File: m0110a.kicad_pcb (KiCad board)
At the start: 2 copper layers, 177 parts, among them SW1 SW_Push, U1 ATmega32U4-AU, Y1 16MHz

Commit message: fix foot print associations. place switch foot prints and some diodes
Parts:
- removed C1, C2: 22pF, Capacitor_SMD:C_0805_2012Metric
- removed C3: 1uF, Capacitor_SMD:C_0805_2012Metric
- removed C4, C5, C6: 0.1uF, Capacitor_SMD:C_0805_2012Metric
- removed C7: 10uF, Capacitor_SMD:C_0805_2012Metric
- removed D80: D_Small, Diode_SMD:D_SOD-123
- removed F1: 500mA, Fuse:Fuse_1206_3216Metric
- removed MX_1, MX_2, MX_3, MX_4, MX_5, MX_6, MX_7, MX_8, MX_9, MX_A1, MX_B1, MX_BSLSH1, MX_C1, MX_COMMA1, MX_D1, MX_DOT1, MX_DWN1, MX_E1, MX_EQL1, MX_ESC1, MX_F1, MX_FN1, MX_G1, MX_H1, MX_I1, MX_J1, MX_K1, MX_L1, MX_LBRC1, MX_LEFT1, MX_M1, MX_MINS1, MX_N1, MX_NUM1, MX_NUM_0, MX_NUM_1, MX_NUM_2, MX_NUM_3, MX_NUM_4, MX_NUM_5, MX_NUM_6, MX_NUM_7, MX_NUM_8, MX_NUM_9, MX_NUM_ADD1, MX_NUM_DBL_0, MX_NUM_DOT1, MX_NUM_EQL1, MX_NUM_MINS1, MX_NUM_MUL1, MX_NUM_SLSH1, MX_O1, MX_P1, MX_Q1, MX_QUOT1, MX_R1, MX_RBRC1, MX_RIGHT1, MX_S1, MX_SEMI1, MX_SLSH1, MX_T1, MX_U1, MX_UP1, MX_V1, MX_W1, MX_X1, MX_Y1, MX_Z1, MX_ZERO1: MX-LED, MX_Alps_Hybrid:MX-1U
- removed MX_7U_SPC1: MX-LED, MX_Alps_Hybrid:MX-7U
- removed MX_BSPC1, MX_LALT1, MX_TAB1: MX-LED, MX_Alps_Hybrid:MX-1.5U
- removed MX_CAP1, MX_ENTER1: MX-LED, MX_Alps_Hybrid:MX-1.75U
- removed MX_LGUI1, MX_NUM_BIG_0, MX_NUM_ENT1: MX-LED, MX_Alps_Hybrid:MX-2U
- removed MX_LSFT1: MX-LED, MX_Alps_Hybrid:MX-2.25U
- removed MX_RSFT1: MX-LED, MX_Alps_Hybrid:MX-1.25U
- removed R1, R4: 10k, Resistor_SMD:R_0805_2012Metric
- removed R2, R3: 22, Resistor_SMD:R_0805_2012Metric
- removed SW1: SW_Push, random-keyboard-parts:SKQG-1155865
- removed USB1: Molex-0548190589, random-keyboard-parts:Molex-0548190589
- removed Y1: 16MHz, Crystal:Crystal_SMD_3225-4Pin_3.2x2.5mm
- added MX1: CherryMX_LTST-A683CEGBW, CherryMX_PCB_KailhSocket_LTST-A683CEGBW:CherryMX_1.00u_PCB_KailhSocket_LTST-A683CEGBW, F.Cu at (95.2, 0.00)
- added MX10: CherryMX_LTST-A683CEGBW, CherryMX_PCB_KailhSocket_LTST-A683CEGBW:CherryMX_1.00u_PCB_KailhSocket_LTST-A683CEGBW, F.Cu at (57.1, 0.00)
- added MX11: CherryMX_LTST-A683CEGBW, CherryMX_PCB_KailhSocket_LTST-A683CEGBW:CherryMX_1.00u_PCB_KailhSocket_LTST-A683CEGBW, F.Cu at (209.6, 0.00)
- added MX12: CherryMX_LTST-A683CEGBW, CherryMX_PCB_KailhSocket_LTST-A683CEGBW:CherryMX_1.50u_PCB_KailhSocket_LTST-A683CEGBW, F.Cu at (252.4, 0.00)
- added MX13: CherryMX_LTST-A683CEGBW, CherryMX_PCB_KailhSocket_LTST-A683CEGBW:CherryMX_1.00u_PCB_KailhSocket_LTST-A683CEGBW, F.Cu at (301.6, 0.00)
- added MX14: CherryMX_LTST-A683CEGBW, CherryMX_PCB_KailhSocket_LTST-A683CEGBW:CherryMX_1.00u_PCB_KailhSocket_LTST-A683CEGBW, F.Cu at (339.7, 0.00)
- added MX15: CherryMX_LTST-A683CEGBW, CherryMX_PCB_KailhSocket_LTST-A683CEGBW:CherryMX_1.00u_PCB_KailhSocket_LTST-A683CEGBW, F.Cu at (19.1, 0.00)
- added MX16: CherryMX_LTST-A683CEGBW, CherryMX_PCB_KailhSocket_LTST-A683CEGBW:CherryMX_1.00u_PCB_KailhSocket_LTST-A683CEGBW, F.Cu at (38.1, 0.00)
- added MX17: CherryMX_LTST-A683CEGBW, CherryMX_PCB_KailhSocket_LTST-A683CEGBW:CherryMX_1.00u_PCB_KailhSocket_LTST-A683CEGBW, F.Cu at (228.6, 0.00)
- added MX18: CherryMX_LTST-A683CEGBW, CherryMX_PCB_KailhSocket_LTST-A683CEGBW:CherryMX_1.00u_PCB_KailhSocket_LTST-A683CEGBW, F.Cu at (0.00, 0.00)
- added MX19: CherryMX_LTST-A683CEGBW, CherryMX_PCB_KailhSocket_LTST-A683CEGBW:CherryMX_1.00u_PCB_KailhSocket_LTST-A683CEGBW, F.Cu at (104.8, 19.1)
- added MX2: CherryMX_LTST-A683CEGBW, CherryMX_PCB_KailhSocket_LTST-A683CEGBW:CherryMX_1.00u_PCB_KailhSocket_LTST-A683CEGBW, F.Cu at (114.3, 0.00)
- added MX20: CherryMX_LTST-A683CEGBW, CherryMX_PCB_KailhSocket_LTST-A683CEGBW:CherryMX_1.00u_PCB_KailhSocket_LTST-A683CEGBW, F.Cu at (123.8, 19.1)
- added MX21: CherryMX_LTST-A683CEGBW, CherryMX_PCB_KailhSocket_LTST-A683CEGBW:CherryMX_1.00u_PCB_KailhSocket_LTST-A683CEGBW, F.Cu at (142.9, 19.1)
- added MX22: CherryMX_LTST-A683CEGBW, CherryMX_PCB_KailhSocket_LTST-A683CEGBW:CherryMX_1.00u_PCB_KailhSocket_LTST-A683CEGBW, F.Cu at (161.9, 19.1)
- added MX23: CherryMX_LTST-A683CEGBW, CherryMX_PCB_KailhSocket_LTST-A683CEGBW:CherryMX_1.00u_PCB_KailhSocket_LTST-A683CEGBW, F.Cu at (181.0, 19.1)
- added MX24: CherryMX_LTST-A683CEGBW, CherryMX_PCB_KailhSocket_LTST-A683CEGBW:CherryMX_1.00u_PCB_KailhSocket_LTST-A683CEGBW, F.Cu at (200.0, 19.1)
- added MX25: CherryMX_LTST-A683CEGBW, CherryMX_PCB_KailhSocket_LTST-A683CEGBW:CherryMX_1.00u_PCB_KailhSocket_LTST-A683CEGBW, F.Cu at (85.7, 19.1)
- added MX26: CherryMX_LTST-A683CEGBW, CherryMX_PCB_KailhSocket_LTST-A683CEGBW:CherryMX_1.00u_PCB_KailhSocket_LTST-A683CEGBW, F.Cu at (282.6, 19.1)
- added MX27: CherryMX_LTST-A683CEGBW, CherryMX_PCB_KailhSocket_LTST-A683CEGBW:CherryMX_1.00u_PCB_KailhSocket_LTST-A683CEGBW, F.Cu at (320.7, 19.1)
- added MX28: CherryMX_LTST-A683CEGBW, CherryMX_PCB_KailhSocket_LTST-A683CEGBW:CherryMX_1.00u_PCB_KailhSocket_LTST-A683CEGBW, F.Cu at (66.7, 19.1)
- added MX29: CherryMX_LTST-A683CEGBW, CherryMX_PCB_KailhSocket_LTST-A683CEGBW:CherryMX_1.00u_PCB_KailhSocket_LTST-A683CEGBW, F.Cu at (219.1, 19.1)
- added MX3: CherryMX_LTST-A683CEGBW, CherryMX_PCB_KailhSocket_LTST-A683CEGBW:CherryMX_1.00u_PCB_KailhSocket_LTST-A683CEGBW, F.Cu at (133.3, 0.00)
- added MX30: CherryMX_LTST-A683CEGBW, CherryMX_PCB_KailhSocket_LTST-A683CEGBW:CherryMX_1.00u_PCB_KailhSocket_LTST-A683CEGBW, F.Cu at (257.2, 19.1)
- added MX31: CherryMX_LTST-A683CEGBW, CherryMX_PCB_KailhSocket_LTST-A683CEGBW:CherryMX_1.00u_PCB_KailhSocket_LTST-A683CEGBW, F.Cu at (301.6, 19.1)
- added MX32: CherryMX_LTST-A683CEGBW, CherryMX_PCB_KailhSocket_LTST-A683CEGBW:CherryMX_1.00u_PCB_KailhSocket_LTST-A683CEGBW, F.Cu at (339.7, 19.1)
- added MX33: CherryMX_LTST-A683CEGBW, CherryMX_PCB_KailhSocket_LTST-A683CEGBW:CherryMX_1.00u_PCB_KailhSocket_LTST-A683CEGBW, F.Cu at (28.6, 19.1)
- added MX34: CherryMX_LTST-A683CEGBW, CherryMX_PCB_KailhSocket_LTST-A683CEGBW:CherryMX_1.00u_PCB_KailhSocket_LTST-A683CEGBW, F.Cu at (47.6, 19.1)
- added MX35: CherryMX_LTST-A683CEGBW, CherryMX_PCB_KailhSocket_LTST-A683CEGBW:CherryMX_1.00u_PCB_KailhSocket_LTST-A683CEGBW, F.Cu at (238.1, 19.1)
- added MX36: CherryMX_LTST-A683CEGBW, CherryMX_PCB_KailhSocket_LTST-A683CEGBW:CherryMX_1.50u_PCB_KailhSocket_LTST-A683CEGBW, F.Cu at (4.76, 19.1)
- added MX37: CherryMX_LTST-A683CEGBW, CherryMX_PCB_KailhSocket_LTST-A683CEGBW:CherryMX_1.00u_PCB_KailhSocket_LTST-A683CEGBW, F.Cu at (147.6, 38.1)
- added MX38: CherryMX_LTST-A683CEGBW, CherryMX_PCB_KailhSocket_LTST-A683CEGBW:CherryMX_1.00u_PCB_KailhSocket_LTST-A683CEGBW, F.Cu at (109.5, 38.1)
- added MX39: CherryMX_LTST-A683CEGBW, CherryMX_PCB_KailhSocket_LTST-A683CEGBW:CherryMX_1.00u_PCB_KailhSocket_LTST-A683CEGBW, F.Cu at (128.6, 38.1)
- added MX4: CherryMX_LTST-A683CEGBW, CherryMX_PCB_KailhSocket_LTST-A683CEGBW:CherryMX_1.00u_PCB_KailhSocket_LTST-A683CEGBW, F.Cu at (152.4, 0.00)
- added MX40: CherryMX_LTST-A683CEGBW, CherryMX_PCB_KailhSocket_LTST-A683CEGBW:CherryMX_1.00u_PCB_KailhSocket_LTST-A683CEGBW, F.Cu at (166.7, 38.1)
- added MX41: CherryMX_LTST-A683CEGBW, CherryMX_PCB_KailhSocket_LTST-A683CEGBW:CherryMX_1.00u_PCB_KailhSocket_LTST-A683CEGBW, F.Cu at (185.7, 38.1)
- added MX42: CherryMX_LTST-A683CEGBW, CherryMX_PCB_KailhSocket_LTST-A683CEGBW:CherryMX_1.00u_PCB_KailhSocket_LTST-A683CEGBW, F.Cu at (204.8, 38.1)
- added MX43: CherryMX_LTST-A683CEGBW, CherryMX_PCB_KailhSocket_LTST-A683CEGBW:CherryMX_1.00u_PCB_KailhSocket_LTST-A683CEGBW, F.Cu at (90.5, 38.1)
- added MX44: CherryMX_LTST-A683CEGBW, CherryMX_PCB_KailhSocket_LTST-A683CEGBW:CherryMX_1.00u_PCB_KailhSocket_LTST-A683CEGBW, F.Cu at (282.6, 38.1)
- added MX45: CherryMX_LTST-A683CEGBW, CherryMX_PCB_KailhSocket_LTST-A683CEGBW:CherryMX_1.00u_PCB_KailhSocket_LTST-A683CEGBW, F.Cu at (320.7, 38.1)
- added MX46: CherryMX_LTST-A683CEGBW, CherryMX_PCB_KailhSocket_LTST-A683CEGBW:CherryMX_1.00u_PCB_KailhSocket_LTST-A683CEGBW, F.Cu at (71.4, 38.1)
- added MX47: CherryMX_LTST-A683CEGBW, CherryMX_PCB_KailhSocket_LTST-A683CEGBW:CherryMX_1.00u_PCB_KailhSocket_LTST-A683CEGBW, F.Cu at (223.8, 38.1)
- added MX48: CherryMX_LTST-A683CEGBW, CherryMX_PCB_KailhSocket_LTST-A683CEGBW:CherryMX_1.75u_PCB_KailhSocket_LTST-A683CEGBW, F.Cu at (250.0, 38.1)
- added MX49: CherryMX_LTST-A683CEGBW, CherryMX_PCB_KailhSocket_LTST-A683CEGBW:CherryMX_1.00u_PCB_KailhSocket_LTST-A683CEGBW, F.Cu at (301.6, 38.1)
- added MX5: CherryMX_LTST-A683CEGBW, CherryMX_PCB_KailhSocket_LTST-A683CEGBW:CherryMX_1.00u_PCB_KailhSocket_LTST-A683CEGBW, F.Cu at (171.4, 0.00)
- added MX50: CherryMX_LTST-A683CEGBW, CherryMX_PCB_KailhSocket_LTST-A683CEGBW:CherryMX_1.00u_PCB_KailhSocket_LTST-A683CEGBW, F.Cu at (339.7, 38.1)
- added MX51: CherryMX_LTST-A683CEGBW, CherryMX_PCB_KailhSocket_LTST-A683CEGBW:CherryMX_1.00u_PCB_KailhSocket_LTST-A683CEGBW, F.Cu at (33.3, 38.1)
- added MX52: CherryMX_LTST-A683CEGBW, CherryMX_PCB_KailhSocket_LTST-A683CEGBW:CherryMX_1.00u_PCB_KailhSocket_LTST-A683CEGBW, F.Cu at (52.4, 38.1)
- added MX53: CherryMX_LTST-A683CEGBW, CherryMX_PCB_KailhSocket_LTST-A683CEGBW:CherryMX_1.75u_PCB_KailhSocket_LTST-A683CEGBW, F.Cu at (7.14, 38.1)
- added MX54: CherryMX_LTST-A683CEGBW, CherryMX_PCB_KailhSocket_LTST-A683CEGBW:CherryMX_1.00u_PCB_KailhSocket_LTST-A683CEGBW, F.Cu at (157.2, 57.1)
- added MX55: CherryMX_LTST-A683CEGBW, CherryMX_PCB_KailhSocket_LTST-A683CEGBW:CherryMX_1.00u_PCB_KailhSocket_LTST-A683CEGBW, F.Cu at (119.1, 57.1)
- added MX56: CherryMX_LTST-A683CEGBW, CherryMX_PCB_KailhSocket_LTST-A683CEGBW:CherryMX_1.00u_PCB_KailhSocket_LTST-A683CEGBW, F.Cu at (138.1, 57.1)
- added MX57: CherryMX_LTST-A683CEGBW, CherryMX_PCB_KailhSocket_LTST-A683CEGBW:CherryMX_1.00u_PCB_KailhSocket_LTST-A683CEGBW, F.Cu at (176.2, 57.1)
- added MX58: CherryMX_LTST-A683CEGBW, CherryMX_PCB_KailhSocket_LTST-A683CEGBW:CherryMX_1.00u_PCB_KailhSocket_LTST-A683CEGBW, F.Cu at (195.3, 57.1)
- added MX59: CherryMX_LTST-A683CEGBW, CherryMX_PCB_KailhSocket_LTST-A683CEGBW:CherryMX_1.00u_PCB_KailhSocket_LTST-A683CEGBW, F.Cu at (214.3, 57.1)
- added MX6: CherryMX_LTST-A683CEGBW, CherryMX_PCB_KailhSocket_LTST-A683CEGBW:CherryMX_1.00u_PCB_KailhSocket_LTST-A683CEGBW, F.Cu at (190.5, 0.00)
- added MX60: CherryMX_LTST-A683CEGBW, CherryMX_PCB_KailhSocket_LTST-A683CEGBW:CherryMX_1.00u_PCB_KailhSocket_LTST-A683CEGBW, F.Cu at (100.0, 57.1)
- added MX61: CherryMX_LTST-A683CEGBW, CherryMX_PCB_KailhSocket_LTST-A683CEGBW:CherryMX_1.00u_PCB_KailhSocket_LTST-A683CEGBW, F.Cu at (257.2, 57.1)
- added MX62: CherryMX_LTST-A683CEGBW, CherryMX_PCB_KailhSocket_LTST-A683CEGBW:CherryMX_1.00u_PCB_KailhSocket_LTST-A683CEGBW, F.Cu at (282.6, 57.1)
- added MX63: CherryMX_LTST-A683CEGBW, CherryMX_PCB_KailhSocket_LTST-A683CEGBW:CherryMX_1.00u_PCB_KailhSocket_LTST-A683CEGBW, F.Cu at (320.7, 57.1)
- added MX64: CherryMX_LTST-A683CEGBW, CherryMX_PCB_KailhSocket_LTST-A683CEGBW:CherryMX_1.00u_PCB_KailhSocket_LTST-A683CEGBW, F.Cu at (81.0, 57.1)
- added MX65: CherryMX_LTST-A683CEGBW, CherryMX_PCB_KailhSocket_LTST-A683CEGBW:CherryMX_1.00u_PCB_KailhSocket_LTST-A683CEGBW, F.Cu at (301.6, 57.1)
- added MX66: CherryMX_LTST-A683CEGBW, CherryMX_PCB_KailhSocket_LTST-A683CEGBW:CherryMX_1.00u_PCB_KailhSocket_LTST-A683CEGBW, F.Cu at (42.9, 57.1)
- added MX67: CherryMX_LTST-A683CEGBW, CherryMX_PCB_KailhSocket_LTST-A683CEGBW:CherryMX_1.00u_PCB_KailhSocket_LTST-A683CEGBW, F.Cu at (61.9, 57.1)
- added MX68: CherryMX_LTST-A683CEGBW, CherryMX_PCB_KailhSocket_LTST-A683CEGBW:CherryMX_1.25u_PCB_KailhSocket_LTST-A683CEGBW, F.Cu at (235.7, 57.1)
- added MX69: CherryMX_LTST-A683CEGBW, CherryMX_PCB_KailhSocket_StabWireBottom_LTST-A683CEGBW:CherryMX_2.25u_PCB_KailhSocket_StabWireBottom_LTST-A683CEGBW, F.Cu at (11.9, 57.1)
- added MX7: CherryMX_LTST-A683CEGBW, CherryMX_PCB_KailhSocket_LTST-A683CEGBW:CherryMX_1.00u_PCB_KailhSocket_LTST-A683CEGBW, F.Cu at (76.2, 0.00)
- added MX70: CherryMX_LTST-A683CEGBW, CherryMX_PCB_KailhSocket_StabWireBottom_LTST-A683CEGBW:CherryMX_2.00u_PCB_KailhSocket_StabWireBottom_LTST-A683CEGBW, F.Cu at (339.7, 66.7)
- added MX71: CherryMX_LTST-A683CEGBW, CherryMX_PCB_KailhSocket_StabWireBottom_LTST-A683CEGBW:CherryMX_7.00u_PCB_KailhSocket_StabWireBottom_LTST-A683CEGBW, F.Cu at (123.8, 76.2)
- added MX72: CherryMX_LTST-A683CEGBW, CherryMX_PCB_KailhSocket_LTST-A683CEGBW:CherryMX_1.00u_PCB_KailhSocket_LTST-A683CEGBW, F.Cu at (200.0, 76.2)
- added MX73: CherryMX_LTST-A683CEGBW, CherryMX_PCB_KailhSocket_LTST-A683CEGBW:CherryMX_1.00u_PCB_KailhSocket_LTST-A683CEGBW, F.Cu at (320.7, 76.2)
- added MX74: CherryMX_LTST-A683CEGBW, CherryMX_PCB_KailhSocket_LTST-A683CEGBW:CherryMX_1.00u_PCB_KailhSocket_LTST-A683CEGBW, F.Cu at (219.1, 76.2)
- added MX75: CherryMX_LTST-A683CEGBW, CherryMX_PCB_KailhSocket_LTST-A683CEGBW:CherryMX_1.00u_PCB_KailhSocket_LTST-A683CEGBW, F.Cu at (257.2, 76.2)
- added MX76: CherryMX_LTST-A683CEGBW, CherryMX_PCB_KailhSocket_StabWireBottom_LTST-A683CEGBW:CherryMX_2.00u_PCB_KailhSocket_StabWireBottom_LTST-A683CEGBW, F.Cu at (292.1, 76.2)
- added MX77: CherryMX_LTST-A683CEGBW, CherryMX_PCB_KailhSocket_StabWireBottom_LTST-A683CEGBW:CherryMX_2.00u_PCB_KailhSocket_StabWireBottom_LTST-A683CEGBW, F.Cu at (38.1, 76.2)
- added MX78: CherryMX_LTST-A683CEGBW, CherryMX_PCB_KailhSocket_LTST-A683CEGBW:CherryMX_1.00u_PCB_KailhSocket_LTST-A683CEGBW, F.Cu at (238.1, 76.2)
- added MX79: CherryMX_LTST-A683CEGBW, CherryMX_PCB_KailhSocket_LTST-A683CEGBW:CherryMX_1.50u_PCB_KailhSocket_LTST-A683CEGBW, F.Cu at (4.76, 76.2)
- added MX8: CherryMX_LTST-A683CEGBW, CherryMX_PCB_KailhSocket_LTST-A683CEGBW:CherryMX_1.00u_PCB_KailhSocket_LTST-A683CEGBW, F.Cu at (282.6, 0.00)
- added MX9: CherryMX_LTST-A683CEGBW, CherryMX_PCB_KailhSocket_LTST-A683CEGBW:CherryMX_1.00u_PCB_KailhSocket_LTST-A683CEGBW, F.Cu at (320.7, 0.00)
- U1: value ATmega32U4-AU -> Teensy++2.0_(C); footprint Package_QFP:TQFP-44_10x10mm_P0.8mm -> teensy:Teensy2.0++; moved to F.Cu
- moved D18 344.5 mm to (7.94, 0.79)
- moved D17 306.4 mm to (27.0, 0.79)
- moved D19 276.1 mm to (272.1, 114.4), turned to 0 degrees
- moved D20 255.1 mm to (272.1, 117.8), turned to 0 degrees
- moved D37 246.8 mm to (249.0, 117.7), turned to 0 degrees
- moved D21 246.3 mm to (278.5, 124.5), turned to 0 degrees
- moved D15 230.2 mm to (65.1, 0.79)
- moved D22 224.1 mm to (272.8, 124.5), turned to 0 degrees
- moved D38 216.8 mm to (243.2, 117.7), turned to 0 degrees
- moved D69 214.9 mm to (123.2, 102.6), turned to 0 degrees
- moved D14 214.3 mm to (46.0, 0.79)
- moved D23 214.1 mm to (278.5, 127.9), turned to 0 degrees
- moved D73 205.5 mm to (128.9, 107.2), turned to 0 degrees
- moved D70 204.6 mm to (140.4, 106.0), turned to 0 degrees
- moved D24 199.7 mm to (278.5, 131.2), turned to 0 degrees
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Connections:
- U1 pad 1: Net-(U1-Pad1) -> GND
- U1 pad 14: +5V -> Net-(U1-Pad14)
- U1 pad 15: GND -> Net-(U1-Pad15)
- U1 pad 2: +5V -> Net-(U1-Pad2)
- U1 pad 21: Net-(U1-Pad21) -> VCC
- U1 pad 22: Net-(U1-Pad22) -> GND
- U1 pad 23: GND -> Net-(U1-Pad23)
- U1 pad 24: +5V -> Net-(U1-Pad24)
- U1 pad 33: Net-(R4-Pad2) -> GND
- U1 pad 34: +5V -> Net-(U1-Pad34)
- U1 pad 35: GND -> Net-(U1-Pad35)
- U1 pad 43: GND -> Net-(U1-Pad43)
- U1 pad 44: +5V -> Net-(U1-Pad44)
- U1 pad 5: GND -> Net-(U1-Pad5)
- U1 pad 7: +5V -> Net-(U1-Pad7)
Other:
- board outline added: 3.4 x 3 mm

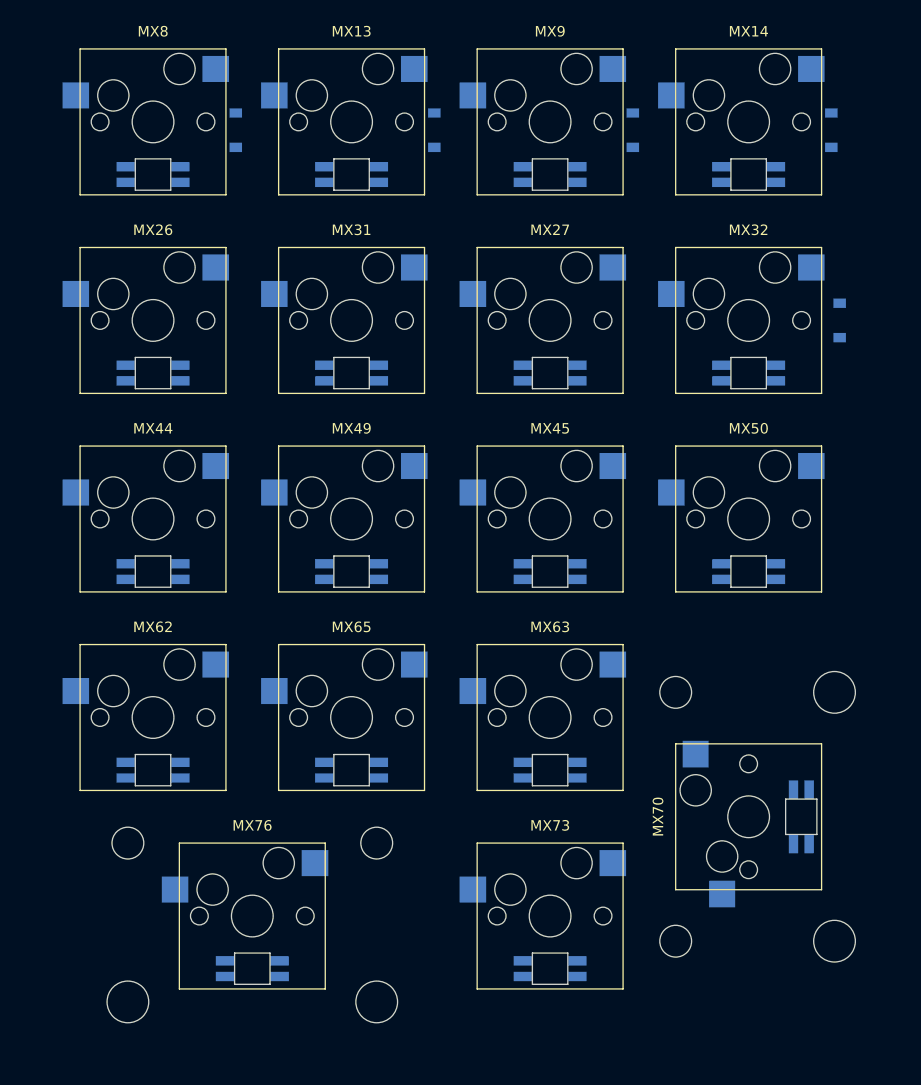
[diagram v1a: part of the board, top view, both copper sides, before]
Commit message: place number pad 34.5mm away from center of back space
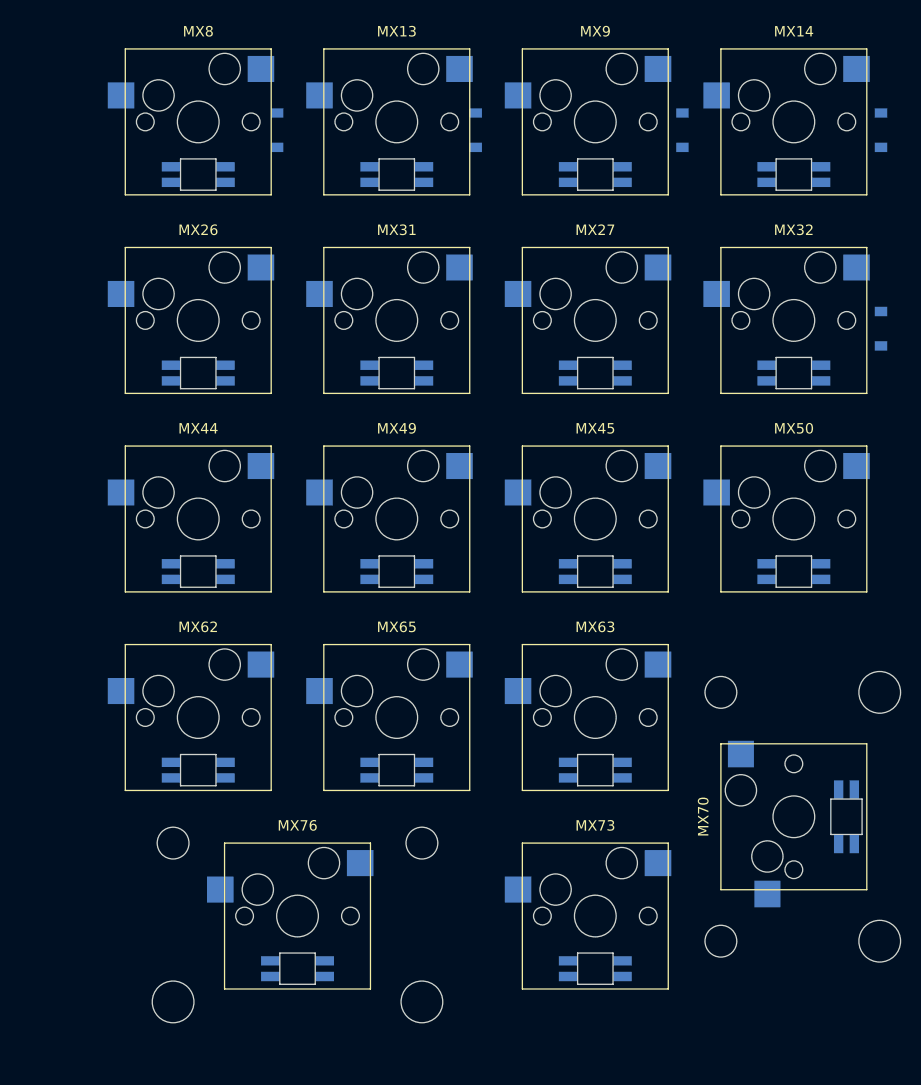
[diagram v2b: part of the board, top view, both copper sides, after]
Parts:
- moved D12 4.76 mm to (352.4, 0.79)
- moved D8 4.76 mm to (333.4, 0.79)
- moved MX26 4.34 mm to (286.9, 19.1)
- moved MX44 4.34 mm to (286.9, 38.1)
- moved MX62 4.34 mm to (286.9, 57.1)
- moved MX8 4.34 mm to (286.9, 0.00)
- moved MX13 4.34 mm to (306.0, 0.00)
- moved MX14 4.34 mm to (344.1, 0.00)
- moved MX27 4.34 mm to (325.0, 19.1)
- moved MX31 4.34 mm to (306.0, 19.1)
- moved MX32 4.34 mm to (344.1, 19.1)
- moved MX45 4.34 mm to (325.0, 38.1)
- moved MX49 4.34 mm to (306.0, 38.1)
- moved MX50 4.34 mm to (344.1, 38.1)
- moved MX63 4.34 mm to (325.0, 57.1)
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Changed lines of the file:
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@@
     (solder_mask_min_width 0.25)
     (aux_axis_origin 0 0)
-    (visible_elements FFFFFF7F)
+    (visible_elements FFFFF77F)
     (pcbplotparams
       (layerselection 0x010fc_ffffffff)
@@
   )
   (module CherryMX_PCB_KailhSocket_StabWireBottom_LTST-A683CEGBW:CherryMX_2.00u_PCB_KailhSocket_StabWireBottom_LTST-A683CEGBW (layer F.Cu)
-    (at 292.1 76.2)
+    (at 296.4375 76.2)
     (descr "Cherry MX switch footprint. Size: 2.00u, Mount type: PCB, Using Kailh Socket: yes, Stabilizer: PCB mounted (Wire Bottom), Lighting: LTST-A683CEGBW")
     (tags "CherryMX 2.00u PCB KailhSocket StabWireBottom LTST-A683CEGBW")
@@
   )
   (module CherryMX_PCB_KailhSocket_StabWireBottom_LTST-A683CEGBW:CherryMX_2.00u_PCB_KailhSocket_StabWireBottom_LTST-A683CEGBW (layer F.Cu)
-    (at 339.725 66.675 90)
+    (at 344.0625 66.675 90)
     (descr "Cherry MX switch footprint. Size: 2.00u, Mount type: PCB, Using Kailh Socket: yes, Stabilizer: PCB mounted (Wire Bottom), Lighting: LTST-A683CEGBW")
     (tags "CherryMX 2.00u PCB KailhSocket StabWireBottom LTST-A683CEGBW")
@@
   )
   (module CherryMX_PCB_KailhSocket_LTST-A683CEGBW:CherryMX_1.00u_PCB_KailhSocket_LTST-A683CEGBW (layer F.Cu)
-    (at 320.675 76.2)
+    (at 325.0125 76.2)
     (descr "Cherry MX switch footprint. Size: 1.00u, Mount type: PCB, Using Kailh Socket: yes, Stabilizer: n/a, Lighting: LTST-A683CEGBW")
     (tags "CherryMX 1.00u PCB KailhSocket LTST-A683CEGBW")
@@
   )
   (module CherryMX_PCB_KailhSocket_LTST-A683CEGBW:CherryMX_1.00u_PCB_KailhSocket_LTST-A683CEGBW (layer F.Cu)
-    (at 301.625 57.15)
+    (at 305.9625 57.15)
     (descr "Cherry MX switch footprint. Size: 1.00u, Mount type: PCB, Using Kailh Socket: yes, Stabilizer: n/a, Lighting: LTST-A683CEGBW")
     (tags "CherryMX 1.00u PCB KailhSocket LTST-A683CEGBW")
@@
   )
   (module CherryMX_PCB_KailhSocket_LTST-A683CEGBW:CherryMX_1.00u_PCB_KailhSocket_LTST-A683CEGBW (layer F.Cu)
-    (at 320.675 57.15)
+    (at 325.0125 57.15)
     (descr "Cherry MX switch footprint. Size: 1.00u, Mount type: PCB, Using Kailh Socket: yes, Stabilizer: n/a, Lighting: LTST-A683CEGBW")
     (tags "CherryMX 1.00u PCB KailhSocket LTST-A683CEGBW")
@@
   )
   (module CherryMX_PCB_KailhSocket_LTST-A683CEGBW:CherryMX_1.00u_PCB_KailhSocket_LTST-A683CEGBW (layer F.Cu)
-    (at 282.575 57.15)
+    (at 286.9125 57.15)
     (descr "Cherry MX switch footprint. Size: 1.00u, Mount type: PCB, Using Kailh Socket: yes, Stabilizer: n/a, Lighting: LTST-A683CEGBW")
     (tags "CherryMX 1.00u PCB KailhSocket LTST-A683CEGBW")
@@
   )
   (module CherryMX_PCB_KailhSocket_LTST-A683CEGBW:CherryMX_1.00u_PCB_KailhSocket_LTST-A683CEGBW (layer F.Cu)
-    (at 339.725 38.1)
+    (at 344.0625 38.1)
     (descr "Cherry MX switch footprint. Size: 1.00u, Mount type: PCB, Using Kailh Socket: yes, Stabilizer: n/a, Lighting: LTST-A683CEGBW")
     (tags "CherryMX 1.00u PCB KailhSocket LTST-A683CEGBW")
@@
   )
   (module CherryMX_PCB_KailhSocket_LTST-A683CEGBW:CherryMX_1.00u_PCB_KailhSocket_LTST-A683CEGBW (layer F.Cu)
-    (at 301.625 38.1)
+    (at 305.9625 38.1)
     (descr "Cherry MX switch footprint. Size: 1.00u, Mount type: PCB, Using Kailh Socket: yes, Stabilizer: n/a, Lighting: LTST-A683CEGBW")
     (tags "CherryMX 1.00u PCB KailhSocket LTST-A683CEGBW")
@@
   )
   (module CherryMX_PCB_KailhSocket_LTST-A683CEGBW:CherryMX_1.00u_PCB_KailhSocket_LTST-A683CEGBW (layer F.Cu)
-    (at 320.675 38.1)
+    (at 325.0125 38.1)
     (descr "Cherry MX switch footprint. Size: 1.00u, Mount type: PCB, Using Kailh Socket: yes, Stabilizer: n/a, Lighting: LTST-A683CEGBW")
     (tags "CherryMX 1.00u PCB KailhSocket LTST-A683CEGBW")
@@
   )
   (module CherryMX_PCB_KailhSocket_LTST-A683CEGBW:CherryMX_1.00u_PCB_KailhSocket_LTST-A683CEGBW (layer F.Cu)
-    (at 282.575 38.1)
+    (at 286.9125 38.1)
     (descr "Cherry MX switch footprint. Size: 1.00u, Mount type: PCB, Using Kailh Socket: yes, Stabilizer: n/a, Lighting: LTST-A683CEGBW")
     (tags "CherryMX 1.00u PCB KailhSocket LTST-A683CEGBW")
@@
   )
   (module CherryMX_PCB_KailhSocket_LTST-A683CEGBW:CherryMX_1.00u_PCB_KailhSocket_LTST-A683CEGBW (layer F.Cu)
-    (at 339.725 19.05)
+    (at 344.0625 19.05)
     (descr "Cherry MX switch footprint. Size: 1.00u, Mount type: PCB, Using Kailh Socket: yes, Stabilizer: n/a, Lighting: LTST-A683CEGBW")
     (tags "CherryMX 1.00u PCB KailhSocket LTST-A683CEGBW")
@@
   )
   (module CherryMX_PCB_KailhSocket_LTST-A683CEGBW:CherryMX_1.00u_PCB_KailhSocket_LTST-A683CEGBW (layer F.Cu)
-    (at 301.625 19.05)
+    (at 305.9625 19.05)
     (descr "Cherry MX switch footprint. Size: 1.00u, Mount type: PCB, Using Kailh Socket: yes, Stabilizer: n/a, Lighting: LTST-A683CEGBW")
     (tags "CherryMX 1.00u PCB KailhSocket LTST-A683CEGBW")
@@
   )
   (module CherryMX_PCB_KailhSocket_LTST-A683CEGBW:CherryMX_1.00u_PCB_KailhSocket_LTST-A683CEGBW (layer F.Cu)
-    (at 320.675 19.05)
+    (at 325.0125 19.05)
     (descr "Cherry MX switch footprint. Size: 1.00u, Mount type: PCB, Using Kailh Socket: yes, Stabilizer: n/a, Lighting: LTST-A683CEGBW")
     (tags "CherryMX 1.00u PCB KailhSocket LTST-A683CEGBW")
@@
   )
   (module CherryMX_PCB_KailhSocket_LTST-A683CEGBW:CherryMX_1.00u_PCB_KailhSocket_LTST-A683CEGBW (layer F.Cu)
-    (at 282.575 19.05)
+    (at 286.9125 19.05)
     (descr "Cherry MX switch footprint. Size: 1.00u, Mount type: PCB, Using Kailh Socket: yes, Stabilizer: n/a, Lighting: LTST-A683CEGBW")
     (tags "CherryMX 1.00u PCB KailhSocket LTST-A683CEGBW")
@@
   )
   (module CherryMX_PCB_KailhSocket_LTST-A683CEGBW:CherryMX_1.00u_PCB_KailhSocket_LTST-A683CEGBW (layer F.Cu)
-    (at 339.725 0)
+    (at 344.0625 0)
     (descr "Cherry MX switch footprint. Size: 1.00u, Mount type: PCB, Using Kailh Socket: yes, Stabilizer: n/a, Lighting: LTST-A683CEGBW")
     (tags "CherryMX 1.00u PCB KailhSocket LTST-A683CEGBW")
@@
   )
   (module CherryMX_PCB_KailhSocket_LTST-A683CEGBW:CherryMX_1.00u_PCB_KailhSocket_LTST-A683CEGBW (layer F.Cu)
-    (at 301.625 0)
+    (at 305.9625 0)
     (descr "Cherry MX switch footprint. Size: 1.00u, Mount type: PCB, Using Kailh Socket: yes, Stabilizer: n/a, Lighting: LTST-A683CEGBW")
     (tags "CherryMX 1.00u PCB KailhSocket LTST-A683CEGBW")
@@
   )
   (module CherryMX_PCB_KailhSocket_LTST-A683CEGBW:CherryMX_1.00u_PCB_KailhSocket_LTST-A683CEGBW (layer F.Cu)
-    (at 320.675 0)
+    (at 325.0125 0)
     (descr "Cherry MX switch footprint. Size: 1.00u, Mount type: PCB, Using Kailh Socket: yes, Stabilizer: n/a, Lighting: LTST-A683CEGBW")
     (tags "CherryMX 1.00u PCB KailhSocket LTST-A683CEGBW")
@@
     )
   )
-  (module CherryMX_PCB_KailhSocket_LTST-A683CEGBW:CherryMX_1.00u_PCB_KailhSocket_LTST-A683CEGBW (layer F.Cu)
-    (at 282.575 0)
+  (module CherryMX_PCB_KailhSocket_LTST-A683CEGBW:CherryMX_1.00u_PCB_KailhSocket_LTST-A683CEGBW locked (layer F.Cu)
+    (at 286.9125 0)
     (descr "Cherry MX switch footprint. Size: 1.00u, Mount type: PCB, Using Kailh Socket: yes, Stabilizer: n/a, Lighting: LTST-A683CEGBW")
     (tags "CherryMX 1.00u PCB KailhSocket LTST-A683CEGBW")
@@
   )
   (module Diode_SMD:D_SOD-123 (layer B.Cu)
-    (at 348.45625 19.05 90)
+    (at 352.425 19.84375 90)
     (descr SOD-123)
     (tags SOD-123)
@@
   )
   (module Diode_SMD:D_SOD-123 (layer B.Cu)
-    (at 347.6625 0.79375 90)
+    (at 352.425 0.79375 90)
     (descr SOD-123)
     (tags SOD-123)
@@
   )
   (module Diode_SMD:D_SOD-123 (layer B.Cu)
-    (at 309.5625 0.79375 90)
+    (at 313.53125 0.79375 90)
     (descr SOD-123)
     (tags SOD-123)
@@
   )
   (module Diode_SMD:D_SOD-123 (layer B.Cu)
-    (at 290.5125 0.79375 90)
+    (at 294.48125 0.79375 90)
     (descr SOD-123)
     (tags SOD-123)
@@
   )
   (module Diode_SMD:D_SOD-123 (layer B.Cu)
-    (at 328.6125 0.79375 90)
+    (at 333.375 0.79375 90)
     (descr SOD-123)
     (tags SOD-123)

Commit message: place diodes
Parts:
- moved D34 292.2 mm to (12.7, 19.8), turned to 90 degrees
- moved D31 267.8 mm to (36.5, 19.8), turned to 90 degrees
- moved D35 248.8 mm to (55.6, 19.8), turned to 90 degrees
- moved D20 220.4 mm to (74.6, 19.8), turned to 90 degrees
- moved D64 214.8 mm to (332.6, 57.9), turned to 90 degrees
- moved D70 210.0 mm to (344.5, 56.4)
- moved D27 205.1 mm to (93.7, 19.8), turned to 90 degrees
- moved D72 200.5 mm to (332.6, 77.0), turned to 90 degrees
- moved D21 196.1 mm to (112.7, 19.8), turned to 90 degrees
- moved D68 190.2 mm to (313.5, 57.9), turned to 90 degrees
- moved D53 189.6 mm to (352.4, 38.9), turned to 90 degrees
- moved D49 177.9 mm to (332.6, 38.9), turned to 90 degrees
- moved D22 175.6 mm to (131.8, 19.8), turned to 90 degrees
- moved D78 174.5 mm to (305.6, 77.0), turned to 90 degrees
- moved D50 172.1 mm to (16.7, 38.9), turned to 90 degrees
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
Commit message: add pcb edge cuts
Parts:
- added H1: MountingHole_Pad, MountingHole:MountingHole_2.5mm_Pad, F.Cu at (117.5, 145.3)
- U1: value Teensy++2.0_(C) -> Teensy2.0_(C); footprint teensy:Teensy2.0++ -> teensy:Teensy2.0; moved to B.Cu
- moved U1 40.0 mm to (94.5, 76.2)
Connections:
- U1 pad 14: Net-(U1-Pad14) -> VCC
- U1 pad 15: Net-(U1-Pad15) -> GND
- U1 pad 21: VCC -> Net-(U1-Pad21)
- U1 pad 22: GND -> Net-(U1-Pad22)
- U1 pad 29: Net-(U1-Pad29) -> VCC
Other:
- board size 3.4 x 3 mm -> 365.1 x 97.6 mm

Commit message: connect first row diodes and rgb data lines
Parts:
- removed H1: MountingHole_Pad, MountingHole:MountingHole_2.5mm_Pad
- moved D4 0.51 mm to (160.1, 1.27)
- moved D15 0.51 mm to (64.9, 1.27)
- moved D1 0.48 mm to (103.1, 1.27)
- moved D3 0.48 mm to (141.2, 1.27)
- moved D5 0.48 mm to (179.5, 1.27)
- moved D6 0.48 mm to (198.4, 1.27)
- moved D9 0.48 mm to (217.4, 1.27)
- moved D18 0.48 mm to (8.00, 1.27)
- moved D10 0.48 mm to (294.5, 1.27)
- moved D11 0.48 mm to (313.5, 1.27)
- moved D12 0.48 mm to (352.4, 1.27)
- moved D13 0.48 mm to (261.9, 1.27)
- moved D14 0.48 mm to (46.0, 1.27)
- moved D16 0.48 mm to (237.3, 1.27)
- moved D17 0.48 mm to (27.0, 1.27)
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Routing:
- net ROW0: track 0.00 -> 344.4 mm
- net Net-(MX12-Pad5): track 0.00 -> 29.9 mm
- net Net-(MX12-Pad4): track 0.00 -> 19.2 mm
- net Net-(MX1-Pad5): track 0.00 -> 14.5 mm
- net Net-(MX1-Pad4): track 0.00 -> 14.5 mm
- net Net-(MX5-Pad5): track 0.00 -> 14.5 mm
- net Net-(MX11-Pad5): track 0.00 -> 14.5 mm
- net Net-(MX11-Pad4): track 0.00 -> 14.5 mm
- net Net-(MX3-Pad5): track 0.00 -> 14.5 mm
- net Net-(MX13-Pad5): track 0.00 -> 14.5 mm
- net Net-(MX13-Pad4): track 0.00 -> 14.5 mm
- net Net-(MX15-Pad5): track 0.00 -> 14.5 mm
- net Net-(MX15-Pad4): track 0.00 -> 14.5 mm
- net Net-(MX4-Pad5): track 0.00 -> 14.5 mm
- net Net-(MX2-Pad5): track 0.00 -> 14.5 mm
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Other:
- net class Default: trace_width 0.25 -> 0.254
- net class Power added: clearance 0.2, trace_width 0.381, via_dia 0.8, via_drill 0.4

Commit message: connect second row's diodes and rgb data lines
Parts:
- moved D24 0.50 mm to (169.4, 20.1)
- moved D25 0.50 mm to (207.5, 20.1)
- moved D26 0.50 mm to (264.7, 20.1)
- moved D29 0.50 mm to (226.6, 20.1)
- moved D20 0.39 mm to (74.3, 20.1)
- moved D22 0.39 mm to (131.4, 20.1)
- moved D27 0.39 mm to (93.3, 20.1)
- moved D28 0.39 mm to (188.6, 20.1)
- moved D30 0.39 mm to (245.7, 20.1)
- moved D21 0.29 mm to (112.5, 20.1)
- moved D35 0.29 mm to (55.4, 20.1)
- moved D23 0.29 mm to (150.6, 20.1)
- moved D19 0.27 mm to (294.6, 20.1)
- moved D32 0.22 mm to (332.6, 20.1)
- moved D34 0.22 mm to (12.7, 20.1)
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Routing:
- net ROW1: track 0.00 -> 340.0 mm
- net Net-(MX26-Pad4): track 0.00 -> 25.2 mm
- net Net-(MX33-Pad4): track 0.00 -> 19.2 mm
- net Net-(MX27-Pad4): track 0.00 -> 14.5 mm
- net Net-(MX23-Pad5): track 0.00 -> 14.5 mm
- net Net-(MX26-Pad5): track 0.00 -> 14.5 mm
- net Net-(MX20-Pad5): track 0.00 -> 14.5 mm
- net Net-(MX28-Pad4): track 0.00 -> 14.5 mm
- net Net-(MX33-Pad5): track 0.00 -> 14.5 mm
- net Net-(MX30-Pad4): track 0.00 -> 14.5 mm
- net Net-(MX29-Pad5): track 0.00 -> 14.5 mm
- net Net-(MX25-Pad4): track 0.00 -> 14.5 mm
- net Net-(MX24-Pad5): track 0.00 -> 14.5 mm
- net Net-(MX22-Pad5): track 0.00 -> 14.5 mm
- net Net-(MX21-Pad5): track 0.00 -> 14.5 mm
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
